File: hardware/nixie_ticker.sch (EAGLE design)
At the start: 69 parts, among them Q1 BCX19SMD, Q2 BCX19SMD

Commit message: Updating 8-12
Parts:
- removed C16: (no value), resistor:C-USC0402
- removed CD40109B: CD40109B, nixie_ticker:CD40109B
- removed JP1: (no value), pinhead:PINHD-1X6
- removed U$1, U$11, U$15, U$19, U$2, U$5: IN14, nixie_ticker:IN14
- removed U$25: UUR1C221MCL6GS, nixie_ticker:UUR1C221MCL6GS
- added JP2: (no value), pinhead:PINHD-1X5
- added L1, L2, L3, L4, L5, L6: (no value), led:LEDSML1206
- added N1, N2, N3, N4, N5, N6: IN14_12PIN12PIN, nixie_ticker:IN14_12PIN12PIN
- added R25, R26, R27, R28, R29, R30: (no value), resistor:R-US_R0805
- C15: value (none) -> 220uF; device resistor:C-USC0402 -> nixie_ticker:UUR1C221MCL6GS
- R17, R18: device resistor:R-US_R0805 -> resistor:R-US_R0402
- R5, R6: device resistor:R-US_R0402 -> resistor:R-US_R0805
- renumbered U$12 to U4, U$16 to U5, U$20 to U6, U$6 to U3, U$7 to U1, U$8 to U2
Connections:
- net N$101 renamed D5I2
- net N$24 renamed D1I1
- net N$25 renamed D1I2
- net N$26 renamed D1I4
- net N$27 renamed D1I8
- net N$28 renamed D1A
- net N$29 renamed D2I1
- net N$30 renamed D2I2
- net N$41 renamed D2I4
- net N$44 renamed D3I1
- net N$45 renamed D3I2
- net N$46 renamed D3I4
- net N$47 renamed D2I8
- net N$48 renamed D3I8
- net N$49 renamed D3A
- net N$50 renamed D4I1
- net N$51 renamed D4I2
- net N$52 renamed D4I4
- net N$53 renamed D4I8
- net N$54 renamed D5I1
- net N$55 renamed D4PR
- net N$56 renamed D4A
- net N$58 renamed D5I4
- net N$59 renamed D5I8
- net N$60 renamed D5A
- net N$85 renamed D6A
- removed net +3V3: C16.1, CD40109B.EN, CD40109B.VCC, JP1.3
- removed net DI_L: CD40109B.C, JP1.6
- removed net DS_1: CD40109B.G, R21.2, U$3.DS
- removed net N$81: U$10.Q4, U6.I1
- removed net N$82: U$10.Q6, U6.I2
- removed net N$83: U$10.Q7, U6.I4
- removed net N$84: U$10.Q5, U6.I8
- removed net SHCP_5V: CD40109B.F, R19.2, U$10.SHCP, U$3.SHCP, U$4.SHCP, U$9.SHCP
- removed net SHCP_L: CD40109B.B, JP1.5
- removed net STCP_5V: CD40109B.E, R20.2, U$10.STCP, U$3.STCP, U$4.STCP, U$9.STCP
- removed net STCP_L: CD40109B.A, JP1.4
- new net CLK: JP2.4, R20.2, U$10.STCP, U$3.STCP, U$4.STCP, U$9.STCP
- new net D2A: U$14.+, U$4.Q3
- new net D2PR: Q1.B, U$4.Q2
- new net D6I1: U$10.Q7, U6.I1
- new net D6I2: U$10.Q5, U6.I2
- new net D6I4: U$10.Q4, U6.I4
- new net D6I8: U$10.Q6, U6.I8
- new net DATA: JP2.5, R16.2, U$3.DS
- new net LATCH: JP2.3, R19.2, U$10.SHCP, U$3.SHCP, U$4.SHCP, U$9.SHCP
- new net N$24: L1.C, R26.1
- new net N$25: L2.A, R26.2
- new net N$26: L2.C, R27.2
- new net N$27: L3.A, R27.1
- new net N$28: L3.C, R28.1
- new net N$29: L1.A, R25.1
- new net N$30: L4.A, R28.2
- new net N$41: L4.C, R29.2
- new net N$44: L6.A, R30.2
- net +5V: now also C1.1, C15.+, C2.1, C3.1, JP2.2, R18.2, R22.2, R24.2; no longer C10.1, C12.1, C14.1, C15.1, CD40109B.VDD, JP1.2, R16.2, R5.2, R6.2, U$25.+
- net GND: now also C15.-, JP2.1, L6.C, R16.1, R17.1, R6.1; no longer C15.2, C16.2, CD40109B.VSS, JP1.1, R14.1, R22.1, R24.1, U$25.-
- net N$1: now also N1.0; no longer U$1.0
- net N$10: now also N1.9; no longer U$1.9
- net N$100: now also N5.9; no longer U$15.9
- net N$104: now also N6.A, R11.1; no longer R13.1, U$19.A
- net N$105: now also N2.A; no longer U$2.A
- net N$108: now also C10.1, R18.1; no longer C2.1, R6.1
- net N$109: now also C8.1, R15.1; no longer C1.1, R5.1
- net N$11: now also N2.0; no longer U$2.0
- net N$110: now also C12.1, R22.1; no longer C3.1, R15.1
- net N$111: now also C14.1, R24.1; no longer C8.1, R16.1
- net N$112: now also R5.2; no longer R7.2
- net N$113: now also R6.2; no longer R8.2
- net N$118: now also N3.A, R5.1; no longer R7.1, U$5.A
- net N$119: now also R7.2; no longer R9.2
- net N$12: now also N2.1; no longer U$2.1
- net N$120: now also R8.2; no longer R10.2
- net N$121: now also N6.0; no longer U$19.0
- net N$122: now also N6.1; no longer U$19.1
- net N$123: now also N6.2; no longer U$19.2
- net N$124: now also N6.3; no longer U$19.3
- net N$125: now also N6.4; no longer U$19.4
- net N$126: now also N6.5; no longer U$19.5
- net N$127: now also N6.6; no longer U$19.6
- net N$128: now also N6.7; no longer U$19.7
- net N$129: now also N6.8; no longer U$19.8
- net N$13: now also N2.2; no longer U$2.2
- net N$130: now also N6.9; no longer U$19.9
- net N$14: now also N2.3; no longer U$2.3
- net N$145: now also N4.A, R7.1; no longer R9.1, U$11.A
- net N$146: now also R9.2; no longer R11.2
- net N$147: now also R10.2; no longer R12.2
- net N$15: now also N2.4; no longer U$2.4
- net N$153: now also R11.2; no longer R13.2
- net N$154: now also R12.2; no longer R14.2
- net N$16: now also N2.5; no longer U$2.5
- net N$160: now also R13.1; no longer R18.1
- net N$161: now also R14.1; no longer R17.1
- net N$162: now also N4.PR, R14.2; no longer R17.2, U$11.PR
- net N$163: now also N2.PR, R13.2; no longer R18.2, U$2.PR
- net N$17: now also N2.6; no longer U$2.6
- net N$18: now also N2.7; no longer U$2.7
- net N$19: now also N2.8; no longer U$2.8
- net N$2: now also N1.1; no longer U$1.1
- net N$20: now also N2.9; no longer U$2.9
- net N$21: now also R21.2; no longer R23.2
- net N$22: now also R17.2; no longer R22.2
- net N$23: now also R23.2; no longer R24.2
- net N$3: now also N1.2; no longer U$1.2
- net N$31: now also N3.0; no longer U$5.0
- net N$32: now also N3.1; no longer U$5.1
- net N$33: now also N3.2; no longer U$5.2
- net N$34: now also N3.3; no longer U$5.3
- net N$35: now also N3.4; no longer U$5.4
- net N$36: now also N3.5; no longer U$5.5
- net N$37: now also N3.6; no longer U$5.6
- net N$38: now also N3.7; no longer U$5.7
- net N$39: now also N3.8; no longer U$5.8
- net N$4: now also N1.3; no longer U$1.3
- net N$40: now also N3.9; no longer U$5.9
- net N$42: now also L5.A, R29.1; no longer Q1.B, U$4.Q3
- net N$43: now also L5.C, R30.1; no longer U$14.+, U$4.Q2
- net N$5: now also N1.4; no longer U$1.4
- net N$57: now also N1.A; no longer U$1.A
- net N$6: now also N1.5; no longer U$1.5
- net N$61: now also N4.0; no longer U$11.0
- net N$62: now also N4.1; no longer U$11.1
- net N$63: now also N4.2; no longer U$11.2
- net N$64: now also N4.3; no longer U$11.3
- net N$65: now also N4.4; no longer U$11.4
- net N$66: now also N4.5; no longer U$11.5
- net N$67: now also N4.6; no longer U$11.6
- net N$68: now also N4.7; no longer U$11.7
- net N$69: now also N4.8; no longer U$11.8
- net N$7: now also N1.6; no longer U$1.6
- net N$70: now also N4.9; no longer U$11.9
- net N$8: now also N1.7; no longer U$1.7
- net N$9: now also N1.8; no longer U$1.8
- net N$90: now also N5.A, R9.1; no longer R11.1, U$15.A
- net N$91: now also N5.0; no longer U$15.0
- net N$92: now also N5.1; no longer U$15.1
- net N$93: now also N5.2; no longer U$15.2
- net N$94: now also N5.3; no longer U$15.3
- net N$95: now also N5.4; no longer U$15.4
- net N$96: now also N5.5; no longer U$15.5
- net N$97: now also N5.6; no longer U$15.6
- net N$98: now also N5.7; no longer U$15.7
- net N$99: now also N5.8; no longer U$15.8
- net V+: now also R25.2
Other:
- moved on the sheet: C1, C10, C11, C12, C13, C14, C15, C2, C3, C4, C5, C6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

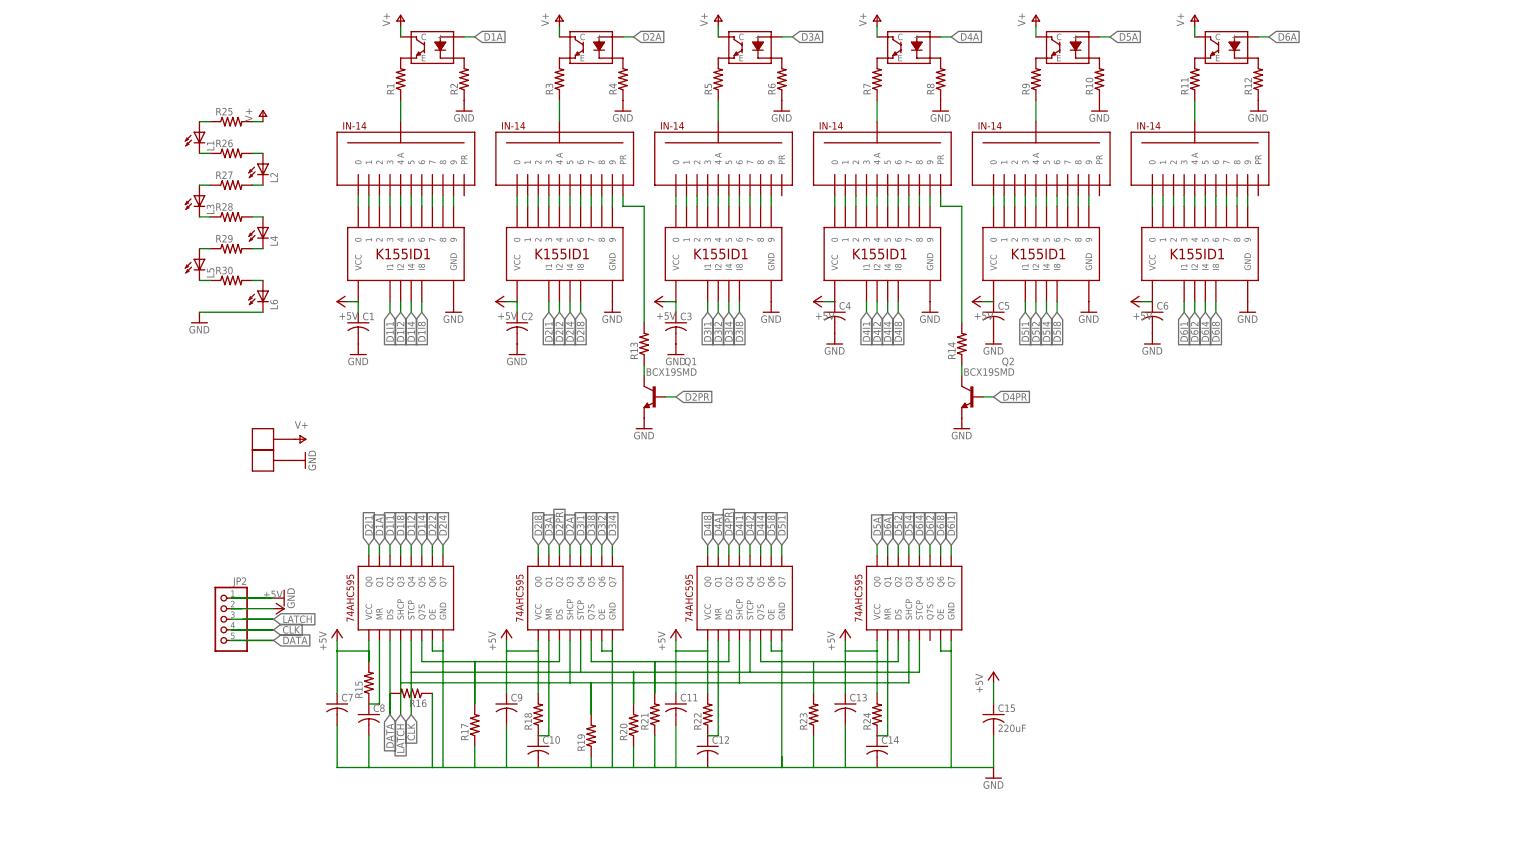
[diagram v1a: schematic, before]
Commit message: Updates 8-17, adding fifth shift register
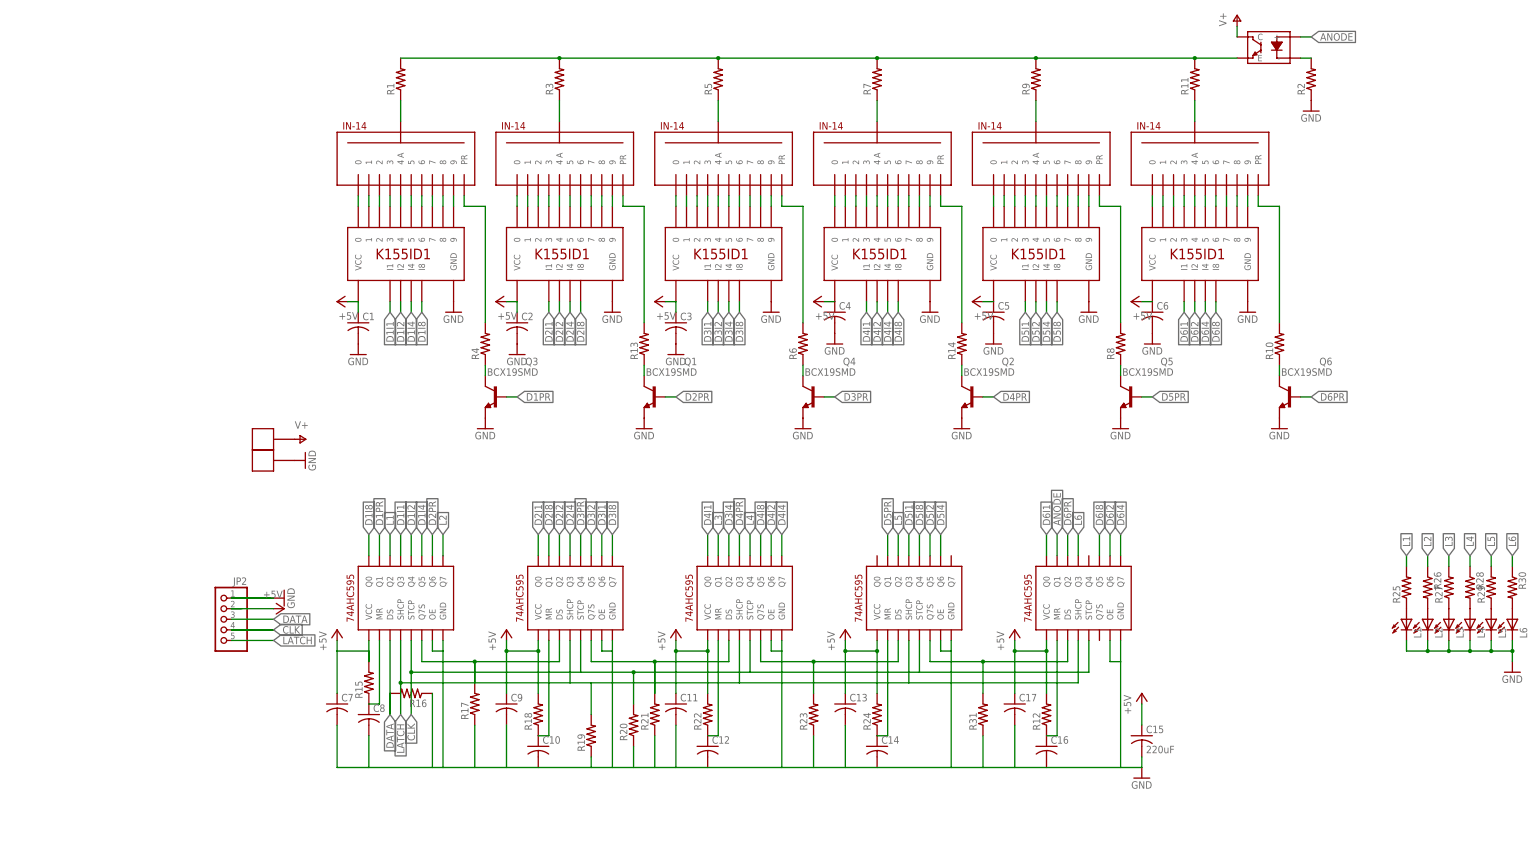
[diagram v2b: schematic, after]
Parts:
- removed U$14, U$18, U$21, U$22, U$23: TLP3873D, nixie_ticker:TLP3873D
- added C16, C17: (no value), resistor:C-USC0402
- added Q3, Q4, Q5, Q6: BCX19SMD, transistor-npn:BCX19SMD
- added R31: (no value), resistor:R-US_R0402
- added U$1: 74AHC595, nixie_ticker:74AHC595
- R12: device resistor:R-US_R0805 -> resistor:R-US_R0402
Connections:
- removed net D1A: U$13.+, U$3.Q1
- removed net D2A: U$14.+, U$4.Q3
- removed net D3A: U$18.+, U$4.Q1
- removed net D4A: U$21.+, U$9.Q1
- removed net D5A: U$10.Q0, U$22.+
- removed net D6A: U$10.Q1, U$23.+
- removed net N$106: R3.2, U$14.E
- removed net N$107: R4.2, U$14.-
- removed net N$112: R5.2, U$18.E
- removed net N$113: R6.2, U$18.-
- removed net N$119: R7.2, U$21.E
- removed net N$120: R8.2, U$21.-
- removed net N$146: R9.2, U$22.E
- removed net N$147: R10.2, U$22.-
- removed net N$153: R11.2, U$23.E
- removed net N$154: R12.2, U$23.-
- removed net N$28: L3.C, R28.1
- removed net N$41: L4.C, R29.2
- removed net N$43: L5.C, R30.1
- new net ANODE: U$1.Q1, U$13.+
- new net D1PR: Q3.B, U$3.Q1
- new net D3PR: Q4.B, U$4.Q4
- new net D5PR: Q5.B, U$10.Q1
- new net D6PR: Q6.B, U$1.Q2
- new net L1: R25.2, U$3.Q2
- new net L2: R26.1, U$3.Q7
- new net L3: R27.2, U$9.Q1
- new net L4: R28.1, U$9.Q4
- new net L5: R29.2, U$10.Q2
- new net L6: R30.1, U$1.Q3
- new net N$45: N1.PR, R4.2
- new net N$46: Q3.C, R4.1
- new net N$47: N3.PR, R6.2
- new net N$48: Q4.C, R6.1
- new net N$49: N5.PR, R8.2
- new net N$50: Q5.C, R8.1
- new net N$51: N6.PR, R10.2
- new net N$52: Q6.C, R10.1
- net +5V: now also C17.1, R12.2, U$1.VCC
- net CLK: now also U$1.STCP
- net D1I1: now also U$3.Q3; no longer U$3.Q2
- net D1I8: now also U$3.Q0; no longer U$3.Q3
- net D2I1: now also U$4.Q0; no longer U$3.Q0
- net D2I2: now also U$4.Q2; no longer U$3.Q6
- net D2I4: now also U$4.Q3; no longer U$3.Q7
- net D2I8: now also U$4.Q1; no longer U$4.Q0
- net D2PR: now also U$3.Q6; no longer U$4.Q2
- net D3I1: now also U$4.Q6; no longer U$4.Q4
- net D3I2: now also U$4.Q5; no longer U$4.Q6
- net D3I4: now also U$9.Q2; no longer U$4.Q7
- net D3I8: now also U$4.Q7; no longer U$4.Q5
- net D4I1: now also U$9.Q0; no longer U$9.Q3
- net D4I2: now also U$9.Q6; no longer U$9.Q4
- net D4I4: now also U$9.Q7; no longer U$9.Q5
- net D4I8: now also U$9.Q5; no longer U$9.Q0
- net D4PR: now also U$9.Q3; no longer U$9.Q2
- net D5I1: now also U$10.Q3; no longer U$9.Q7
- net D5I2: now also U$10.Q5; no longer U$10.Q2
- net D5I4: now also U$10.Q6; no longer U$10.Q3
- net D5I8: now also U$10.Q4; no longer U$9.Q6
- net D6I1: now also U$1.Q0; no longer U$10.Q7
- net D6I2: now also U$1.Q6; no longer U$10.Q5
- net D6I4: now also U$1.Q7; no longer U$10.Q4
- net D6I8: now also U$1.Q5; no longer U$10.Q6
- net DATA: now also JP2.3; no longer JP2.5
- net GND: now also C16.2, C17.2, L1.C, L2.C, L3.C, L4.C, L5.C, Q3.E, Q4.E, Q5.E, Q6.E, R31.1, U$1.GND, U$1.OE; no longer R10.1, R12.1, R4.1, R6.1, R8.1
- net LATCH: now also JP2.5, U$1.SHCP; no longer JP2.3
- net N$102: now also R11.2, R3.2, R5.2, R7.2, R9.2
- net N$24: now also R31.2, U$1.DS, U$10.Q7S; no longer L1.C, R26.1
- net N$26: now also C16.1, R12.1, U$1.MR; no longer L2.C, R27.2
- net V+: no longer R25.2, U$14.C, U$18.C, U$21.C, U$22.C, U$23.C
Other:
- moved on the sheet: C15, L1, L2, L3, L4, L5, L6, R10, R12, R17, R2, R25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

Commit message: Final update before submitting to PCB shop
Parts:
- removed L1, L2, L3, L4, L5, L6: (no value), led:LEDSML1206
- removed U$13: TLP3873D, nixie_ticker:TLP3873D
- removed U$17, U$24: ZKFDS, nixie_ticker:ZKFDS
- added JP1: (no value), pinhead:PINHD-1X5
- added JP3: ZKFDS, nixie_ticker:ZKFDS
- added LED1, LED2, LED3, LED4, LED5, LED6: (no value), led:LEDCHIP-LED0603
- added U7: K155ID1, nixie_ticker:K155ID1
- C1, C2, C3, C4, C5, C6: value (none) -> 1uF
- C15: value 220uF -> (none); device nixie_ticker:UUR1C221MCL6GS -> resistor:C-USC0402
- C17: value (none) -> 220uF; device resistor:C-USC0402 -> nixie_ticker:UUR1C221MCL6GS
- JP2: value (none) -> ZKFDS; device pinhead:PINHD-1X5 -> nixie_ticker:ZKFDS
- R1, R2, R3, R4, R5, R6: value (none) -> 22k; device resistor:R-US_R0805 -> resistor:R-US_R1206
- R10, R11, R13, R20, R23, R8, R9: value (none) -> 10k
- R12: value (none) -> 10k; device resistor:R-US_R0402 -> resistor:R-US_R0805
- R15, R16, R17, R18, R19: device resistor:R-US_R0402 -> resistor:R-US_R0805
- R21, R22, R24, R31: value (none) -> 100k
- R25, R27, R29: value (none) -> 10k; device resistor:R-US_R0805 -> resistor:R-US_R0402
- R26, R28, R30: value (none) -> 100k; device resistor:R-US_R0805 -> resistor:R-US_R0402
- R7: value (none) -> 750; device resistor:R-US_R0805 -> resistor:R-US_R0603
- U1: value K155ID1 -> TLP3873D; device nixie_ticker:K155ID1 -> nixie_ticker:TLP3873D
- renumbered U$1 to U12, U$10 to U11, U$3 to U8, U$4 to U9, U$9 to U10
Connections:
- net +5V: now also C10.1, C17.+, C8.1, JP1.2, R20.2, R23.2, R25.2, R27.2, R29.2, U7.VCC; no longer C13.1, C15.+, C17.1, JP2.2, R12.2, R15.2, R18.2, R22.2, R24.2, U1.VCC
- net ANODE: now also U1.+, U12.Q3; no longer U$13.+, U12.Q1
- net CLK: now also JP1.4, R30.2; no longer JP2.4, R20.2
- net D1I1: now also U2.I1; no longer U1.I1
- net D1I2: now also U2.I2; no longer U1.I2
- net D1I4: now also U2.I4; no longer U1.I4
- net D1I8: now also U2.I8; no longer U1.I8
- net D1PR: now also Q1.B; no longer Q3.B
- net D2I1: now also U3.I1; no longer U2.I1
- net D2I2: now also U3.I2; no longer U2.I2
- net D2I4: now also U3.I4; no longer U2.I4
- net D2I8: now also U3.I8; no longer U2.I8
- net D2PR: now also Q2.B; no longer Q1.B
- net D3I1: now also U4.I1; no longer U3.I1
- net D3I2: now also U4.I2; no longer U3.I2
- net D3I4: now also U4.I4; no longer U3.I4
- net D3I8: now also U4.I8; no longer U3.I8
- net D3PR: now also Q3.B; no longer Q4.B
- net D4I1: now also U5.I1; no longer U4.I1
- net D4I2: now also U5.I2; no longer U4.I2
- net D4I4: now also U5.I4; no longer U4.I4
- net D4I8: now also U5.I8; no longer U4.I8
- net D4PR: now also Q4.B; no longer Q2.B
- net D5I1: now also U6.I1; no longer U5.I1
- net D5I2: now also U6.I2; no longer U5.I2
- net D5I4: now also U6.I4; no longer U5.I4
- net D5I8: now also U6.I8; no longer U5.I8
- net D6I1: now also U7.I1; no longer U6.I1
- net D6I2: now also U7.I2; no longer U6.I2
- net D6I4: now also U7.I4; no longer U6.I4
- net D6I8: now also U7.I8; no longer U6.I8
- net D6PR: now also U12.Q1; no longer U12.Q2
- net DATA: now also JP1.3, R21.2; no longer JP2.3, R16.2
- net GND: now also C15.2, C17.-, JP1.1, JP3.P$1, LED1.C, LED2.C, LED3.C, LED4.C, LED5.C, LED6.C, R22.1, R24.1, R26.1, R28.1, R30.1, R7.1, U7.GND; no longer C15.-, C17.2, JP2.1, L1.C, L2.C, L3.C, L4.C, L5.C, L6.C, R16.1, R17.1, R19.1, R2.1, R20.1, R23.1, U$24.P$1, U1.GND
- net L1: now also R14.2; no longer R25.2
- net L2: now also R15.1; no longer R26.1
- net L3: now also R16.2; no longer R27.2
- net L4: now also R17.1; no longer R28.1
- net L5: now also R18.2; no longer R29.2
- net L6: now also R19.1, U12.Q2; no longer R30.1, U12.Q3
- net LATCH: now also JP1.5, R31.2; no longer JP2.5, R19.2
- net N$1: now also U2.0; no longer U1.0
- net N$10: now also U2.9; no longer U1.9
- net N$100: now also U6.9; no longer U5.9
- net N$102: now also R2.2, R4.2, R6.2, U1.E; no longer R11.2, R7.2, R9.2, U$13.E
- net N$103: now also R7.2, U1.-; no longer R2.2, U$13.-
- net N$104: now also R6.1; no longer R11.1
- net N$105: now also R2.1; no longer R3.1
- net N$108: now also C14.1, R23.1; no longer C10.1, R18.1
- net N$109: now also C12.1, R20.1; no longer C8.1, R15.1
- net N$11: now also U3.0; no longer U2.0
- net N$110: now also C15.1, R25.1; no longer C12.1, R22.1
- net N$111: now also C16.1, R27.1; no longer C14.1, R24.1
- net N$118: now also R3.1; no longer R5.1
- net N$12: now also U3.1; no longer U2.1
- net N$121: now also U7.0; no longer U6.0
- net N$122: now also U7.1; no longer U6.1
- net N$123: now also U7.2; no longer U6.2
- net N$124: now also U7.3; no longer U6.3
- net N$125: now also U7.4; no longer U6.4
- net N$126: now also U7.5; no longer U6.5
- net N$127: now also U7.6; no longer U6.6
- net N$128: now also U7.7; no longer U6.7
- net N$129: now also U7.8; no longer U6.8
- net N$13: now also U3.2; no longer U2.2
- net N$130: now also U7.9; no longer U6.9
- net N$14: now also U3.3; no longer U2.3
- net N$145: now also R4.1; no longer R7.1
- net N$15: now also U3.4; no longer U2.4
- net N$16: now also U3.5; no longer U2.5
- net N$160: now also Q2.C, R9.1; no longer Q1.C, R13.1
- net N$161: now also Q4.C, R11.1; no longer Q2.C, R14.1
- net N$162: now also R11.2; no longer R14.2
- net N$163: now also R9.2; no longer R13.2
- net N$17: now also U3.6; no longer U2.6
- net N$18: now also U3.7; no longer U2.7
- net N$19: now also U3.8; no longer U2.8
- net N$2: now also U2.1; no longer U1.1
- net N$20: now also U3.9; no longer U2.9
- net N$21: now also R24.2; no longer R21.2
- net N$22: now also R22.2; no longer R17.2
- net N$23: now also R26.2; no longer R23.2
- net N$24: now also R28.2; no longer R31.2
- net N$25: now also LED2.A, R15.2; no longer L2.A, R26.2
- net N$26: now also C13.1, R29.1; no longer C16.1, R12.1
- net N$27: now also LED3.A, R16.1; no longer L3.A, R27.1
- net N$29: now also LED1.A, R14.1; no longer L1.A, R25.1
- net N$3: now also U2.2; no longer U1.2
- net N$30: now also LED4.A, R17.2; no longer L4.A, R28.2
- net N$31: now also U4.0; no longer U3.0
- net N$32: now also U4.1; no longer U3.1
- net N$33: now also U4.2; no longer U3.2
- net N$34: now also U4.3; no longer U3.3
- net N$35: now also U4.4; no longer U3.4
- net N$36: now also U4.5; no longer U3.5
- net N$37: now also U4.6; no longer U3.6
- net N$38: now also U4.7; no longer U3.7
- net N$39: now also U4.8; no longer U3.8
- net N$4: now also U2.3; no longer U1.3
- net N$40: now also U4.9; no longer U3.9
- net N$42: now also LED5.A, R18.1; no longer L5.A, R29.1
- net N$44: now also LED6.A, R19.2; no longer L6.A, R30.2
- net N$45: now also R8.2; no longer R4.2
- net N$46: now also Q1.C, R8.1; no longer Q3.C, R4.1
- net N$47: now also R10.2; no longer R6.2
- net N$48: now also Q3.C, R10.1; no longer Q4.C, R6.1
- net N$49: now also R12.2; no longer R8.2
- net N$5: now also U2.4; no longer U1.4
- net N$50: now also R12.1; no longer R8.1
- net N$51: now also R13.2; no longer R10.2
- net N$52: now also R13.1; no longer R10.1
- net N$6: now also U2.5; no longer U1.5
- net N$61: now also U5.0; no longer U4.0
- net N$62: now also U5.1; no longer U4.1
- net N$63: now also U5.2; no longer U4.2
- net N$64: now also U5.3; no longer U4.3
- net N$65: now also U5.4; no longer U4.4
- net N$66: now also U5.5; no longer U4.5
- net N$67: now also U5.6; no longer U4.6
- net N$68: now also U5.7; no longer U4.7
- net N$69: now also U5.8; no longer U4.8
- net N$7: now also U2.6; no longer U1.6
- net N$70: now also U5.9; no longer U4.9
- net N$8: now also U2.7; no longer U1.7
- net N$9: now also U2.8; no longer U1.8
- net N$90: now also R5.1; no longer R9.1
- net N$91: now also U6.0; no longer U5.0
- net N$92: now also U6.1; no longer U5.1
- net N$93: now also U6.2; no longer U5.2
- net N$94: now also U6.3; no longer U5.3
- net N$95: now also U6.4; no longer U5.4
- net N$96: now also U6.5; no longer U5.5
- net N$97: now also U6.6; no longer U5.6
- net N$98: now also U6.7; no longer U5.7
- net N$99: now also U6.8; no longer U5.8
- net V+: now also JP2.P$1, U1.C; no longer U$13.C, U$17.P$1
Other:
- moved on the sheet: C1, C10, C11, C12, C13, C14, C15, C16, C17, C2, C3, C4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

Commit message: Updates 8-28
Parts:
- C1, C2, C3, C4, C5, C6: device resistor:C-USC0402 -> nixie_ticker:C0402
- C10, C11, C12, C13, C14, C15, C16, C7, C8, C9: value (none) -> C0402; device resistor:C-USC0402 -> nixie_ticker:C0402
- R20, R21, R22, R23, R24, R25, R26, R27, R28, R29, R30, R31: device resistor:R-US_R0402 -> nixie_ticker:R0402
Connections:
- net +5V: now also C1.+, C10.+, C11.+, C2.+, C3.+, C4.+, C5.+, C6.+, C7.+, C8.+, C9.+; no longer C1.1, C10.1, C11.1, C2.1, C3.1, C4.1, C5.1, C6.1, C7.1, C8.1, C9.1
- net GND: now also C1.-, C10.-, C11.-, C12.-, C13.-, C14.-, C15.-, C16.-, C2.-, C3.-, C4.-, C5.-, C6.-, C7.-, C8.-, C9.-; no longer C1.2, C10.2, C11.2, C12.2, C13.2, C14.2, C15.2, C16.2, C2.2, C3.2, C4.2, C5.2, C6.2, C7.2, C8.2, C9.2
- net N$108: now also C14.+; no longer C14.1
- net N$109: now also C12.+; no longer C12.1
- net N$110: now also C15.+; no longer C15.1
- net N$111: now also C16.+; no longer C16.1
- net N$26: now also C13.+; no longer C13.1
